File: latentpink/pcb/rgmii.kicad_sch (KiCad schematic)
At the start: 63 parts, among them J5 0826-1G1T-23-F, U2 XC7K160T-2FBG484C, U21 ECX2-LMV-3CN-125.000-TR, U22 ECS-2016MVQ-250-CN, U64 RCLAMP0514M, U65 RCLAMP0514M, U9 KSZ9031RN

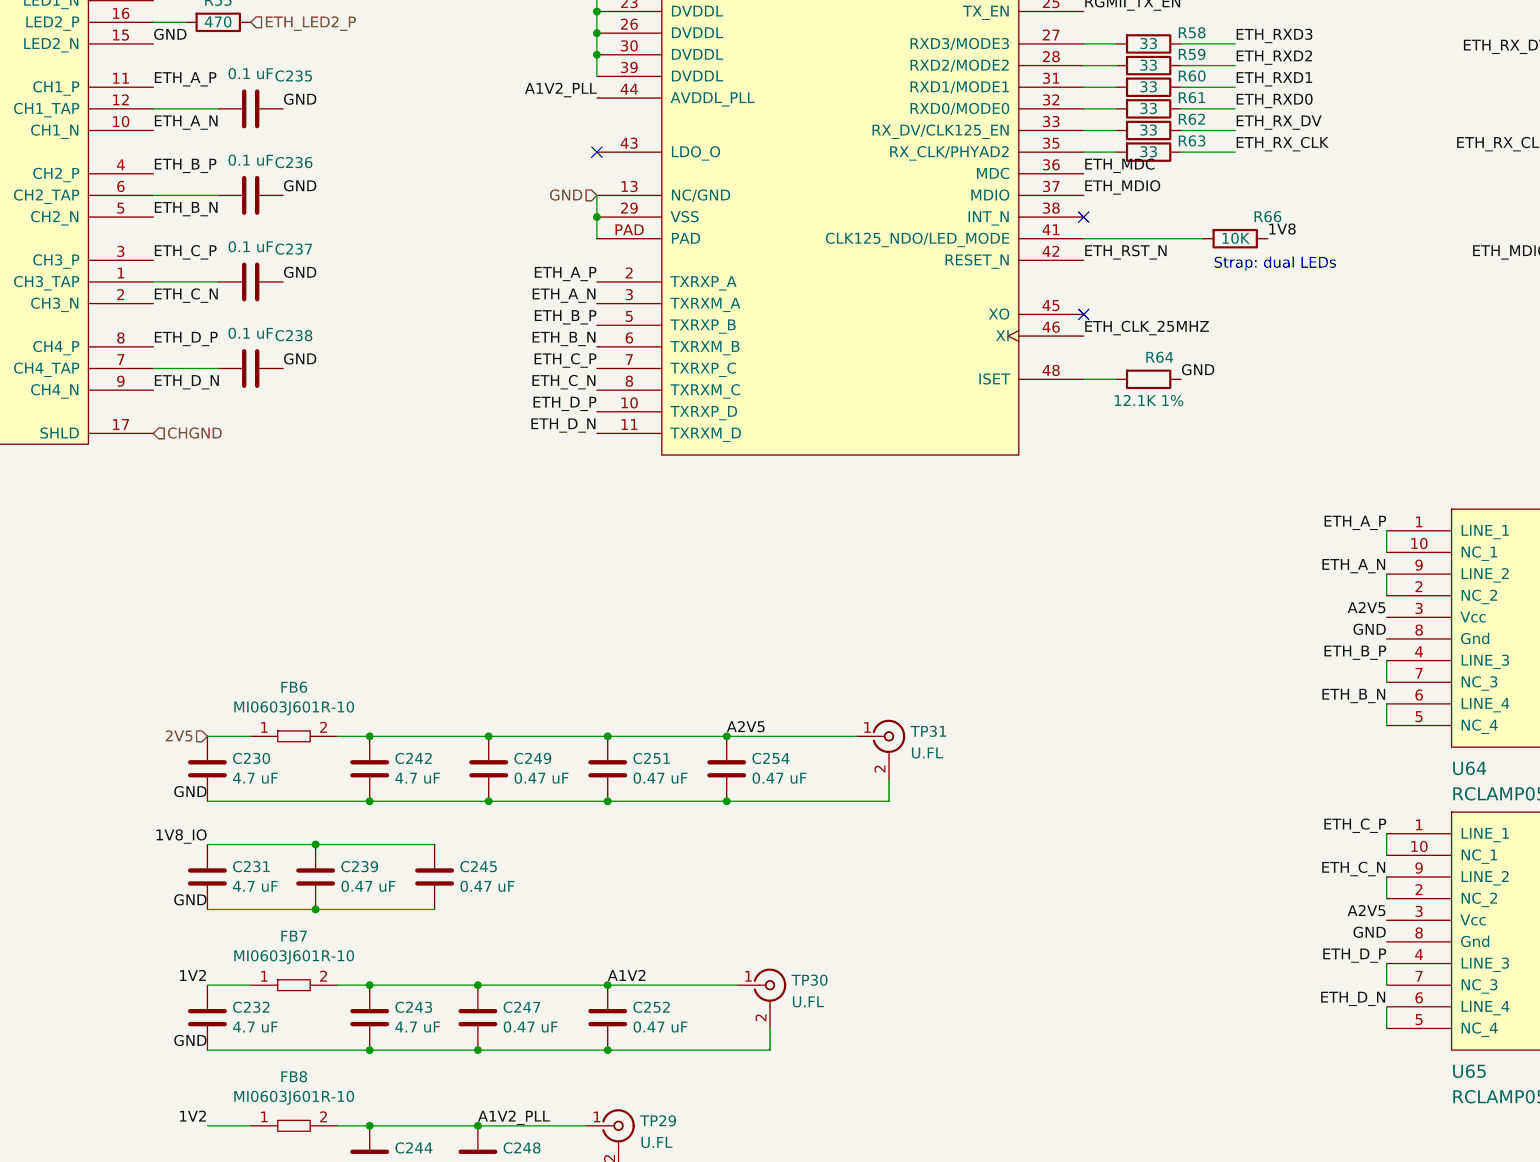
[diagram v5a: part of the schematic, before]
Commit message: Continued PHY layout
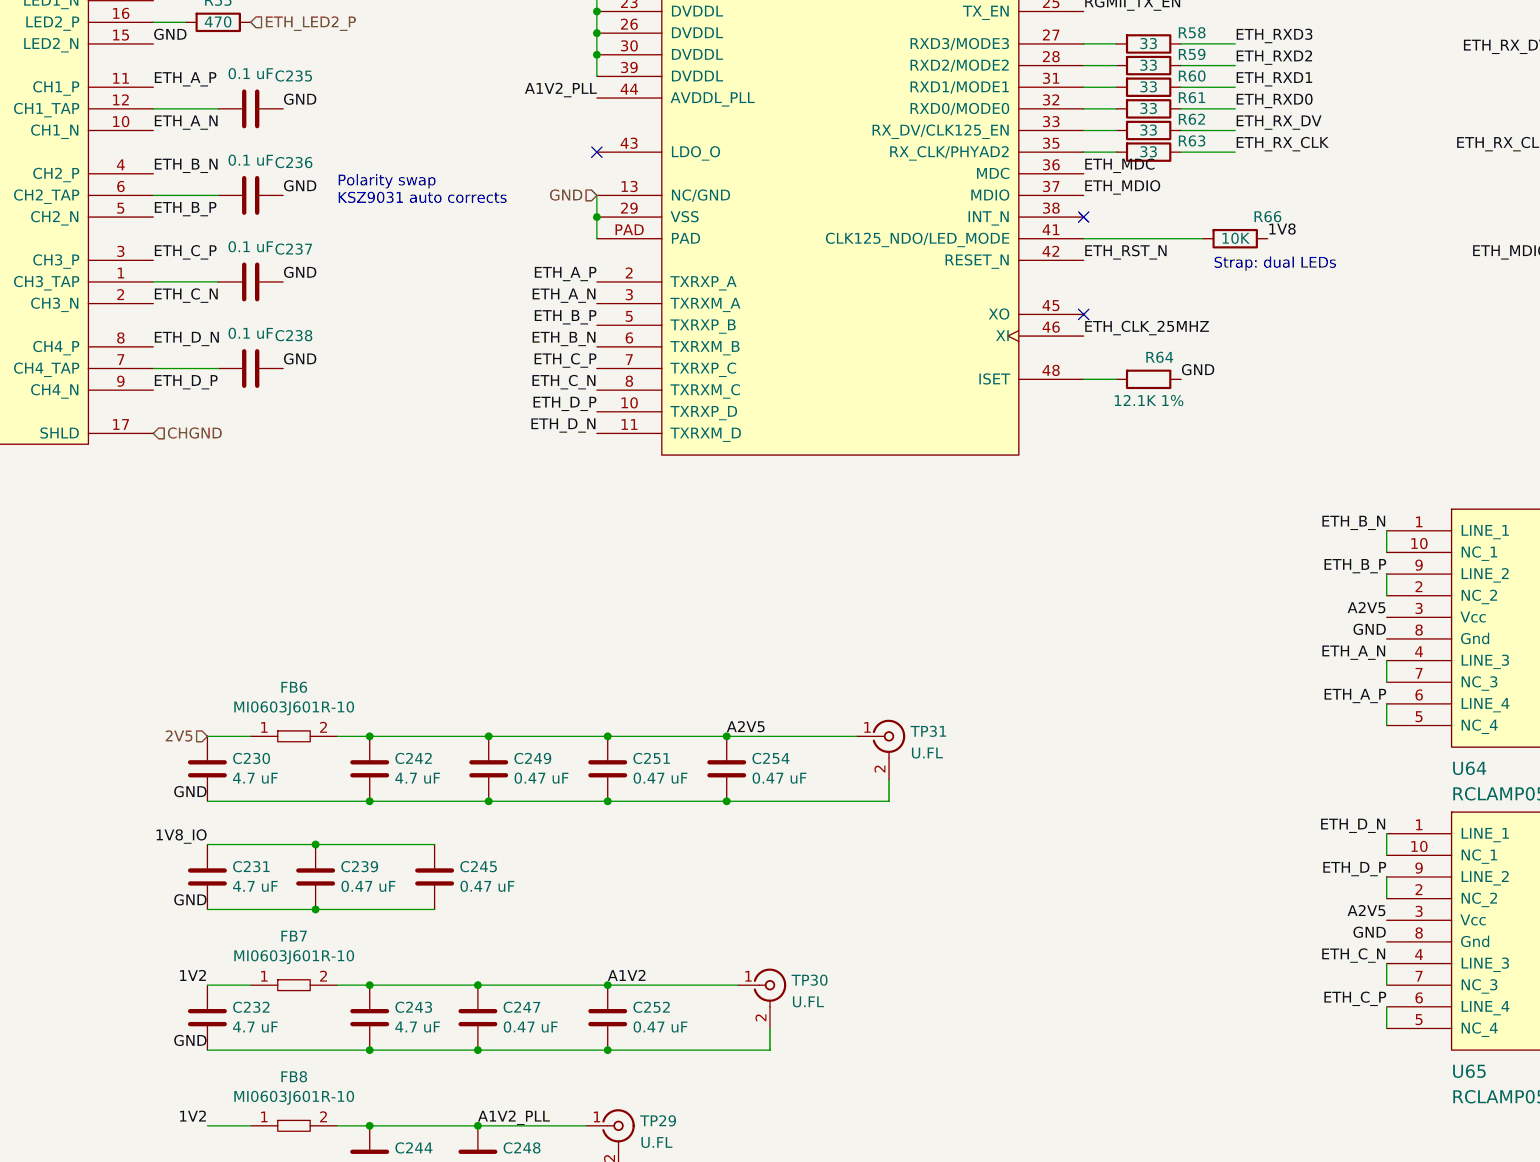
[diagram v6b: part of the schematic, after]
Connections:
- net ETH_A_N: now also U64.4 (LINE_3), U64.7 (NC_3); no longer U64.2 (NC_2), U64.9 (LINE_2)
- net ETH_A_P: now also U64.5 (NC_4), U64.6 (LINE_4); no longer U64.1 (LINE_1), U64.10 (NC_1)
- net ETH_B_N: now also J5.4 (CH2_P), U64.1 (LINE_1), U64.10 (NC_1); no longer J5.5 (CH2_N), U64.5 (NC_4), U64.6 (LINE_4)
- net ETH_B_P: now also J5.5 (CH2_N), U64.2 (NC_2), U64.9 (LINE_2); no longer J5.4 (CH2_P), U64.4 (LINE_3), U64.7 (NC_3)
- net ETH_C_N: now also U65.4 (LINE_3), U65.7 (NC_3); no longer U65.2 (NC_2), U65.9 (LINE_2)
- net ETH_C_P: now also U65.5 (NC_4), U65.6 (LINE_4); no longer U65.1 (LINE_1), U65.10 (NC_1)
- net ETH_D_N: now also J5.8 (CH4_P), U65.1 (LINE_1), U65.10 (NC_1); no longer J5.9 (CH4_N), U65.5 (NC_4), U65.6 (LINE_4)
- net ETH_D_P: now also J5.9 (CH4_N), U65.2 (NC_2), U65.9 (LINE_2); no longer J5.8 (CH4_P), U65.4 (LINE_3), U65.7 (NC_3)
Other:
- note added: "Polarity swap KSZ9031 auto corrects"
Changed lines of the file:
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@@
+    (effects (font (size 1.27 1.27)) (justify left bottom))
+  )
+  (text "Polarity swap\nKSZ9031 auto corrects" (at 64.77 73.66 0)
     (effects (font (size 1.27 1.27)) (justify left bottom))
   )
@@
     (effects (font (size 1.27 1.27)) (justify right bottom))
   )
-  (label "ETH_D_P" (at 187.96 162.56 180)
+  (label "ETH_D_P" (at 187.96 152.4 180)
     (effects (font (size 1.27 1.27)) (justify right bottom))
   )
@@
     (effects (font (size 1.27 1.27)) (justify right bottom))
   )
-  (label "ETH_B_P" (at 187.96 127 180)
-    (effects (font (size 1.27 1.27)) (justify right bottom))
-  )
-  (label "ETH_B_P" (at 43.18 69.85 0)
+  (label "ETH_B_P" (at 187.96 116.84 180)
+    (effects (font (size 1.27 1.27)) (justify right bottom))
+  )
+  (label "ETH_B_P" (at 43.18 74.93 0)
     (effects (font (size 1.27 1.27)) (justify left bottom))
   )
@@
     (effects (font (size 1.27 1.27)) (justify right bottom))
   )
-  (label "ETH_B_N" (at 187.96 132.08 180)
+  (label "ETH_B_N" (at 187.96 111.76 180)
     (effects (font (size 1.27 1.27)) (justify right bottom))
   )
@@
     (effects (font (size 1.27 1.27)) (justify left bottom))
   )
-  (label "ETH_D_N" (at 187.96 167.64 180)
+  (label "ETH_D_N" (at 187.96 147.32 180)
     (effects (font (size 1.27 1.27)) (justify right bottom))
   )
@@
     (effects (font (size 1.27 1.27)) (justify left bottom))
   )
-  (label "ETH_C_N" (at 187.96 152.4 180)
+  (label "ETH_C_N" (at 187.96 162.56 180)
     (effects (font (size 1.27 1.27)) (justify right bottom))
   )
@@
     (effects (font (size 1.27 1.27)) (justify right bottom))
   )
-  (label "ETH_A_N" (at 187.96 116.84 180)
+  (label "ETH_A_N" (at 187.96 127 180)
     (effects (font (size 1.27 1.27)) (justify right bottom))
   )
@@
     (effects (font (size 1.27 1.27)) (justify right bottom))
   )
-  (label "ETH_A_P" (at 187.96 111.76 180)
+  (label "ETH_A_P" (at 187.96 132.08 180)
     (effects (font (size 1.27 1.27)) (justify right bottom))
   )
@@
     (effects (font (size 1.27 1.27)) (justify right bottom))
   )
-  (label "ETH_C_P" (at 187.96 147.32 180)
+  (label "ETH_C_P" (at 187.96 167.64 180)
     (effects (font (size 1.27 1.27)) (justify right bottom))
   )
@@
     (effects (font (size 1.27 1.27)) (justify right bottom))
   )
-  (label "ETH_D_N" (at 43.18 95.25 0)
+  (label "ETH_D_N" (at 43.18 90.17 0)
     (effects (font (size 1.27 1.27)) (justify left bottom))
   )
@@
     (effects (font (size 1.27 1.27)) (justify right bottom))
   )
-  (label "ETH_D_P" (at 43.18 90.17 0)
+  (label "ETH_D_P" (at 43.18 95.25 0)
     (effects (font (size 1.27 1.27)) (justify left bottom))
   )
@@
     (effects (font (size 1.27 1.27)) (justify right bottom))
   )
-  (label "ETH_B_N" (at 43.18 74.93 0)
-    (effects (font (size 1.27 1.27)) (justify left bottom))
-  )
+  (label "ETH_B_N" (at 43.18 69.85 0)
+    (effects (font (size 1.27 1.27)) (justify left bottom))
+  )

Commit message: Lots more layout of low speed stuff and power. Partial layout of 1.2V supply. Initial RGMII escape routing.
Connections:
- net 1V8 is gone; now on net 1V8_IO: R66.1, R67.1, R68.1, R69.1, R73.1
- net ETH_LED1_N_1V8: no longer U2.L3 (IO_L1P_T0_34)
- net ETH_LED2_N_1V8: no longer U2.M3 (IO_L1N_T0_34)
- net ETH_MDC: now also U2.Y2 (IO_L21N_T3_DQS_34); no longer U2.P1 (IO_L8P_T1_34)
- net ETH_MDIO: now also U2.U1 (IO_L10N_T1_34); no longer U2.R1 (IO_L8N_T1_34)
- net ETH_RST_N: now also U2.W1 (IO_L20P_T3_34); no longer U2.M5 (IO_L9P_T1_DQS_34)
- net ETH_RXD0: now also U2.V2 (IO_L15N_T2_DQS_34); no longer U2.P4 (IO_L11P_T1_SRCC_34)
- net ETH_RXD1: now also U2.Y1 (IO_L20N_T3_34); no longer U2.U1 (IO_L10N_T1_34)
- net ETH_RXD2: now also U2.R2 (IO_L7N_T1_34); no longer U2.T1 (IO_L10P_T1_34)
- net ETH_RXD3: now also U2.Y3 (IO_L21P_T3_DQS_34); no longer U2.N4 (IO_L9N_T1_DQS_34)
- net ETH_RX_DV: now also U2.U2 (IO_L15P_T2_DQS_34); no longer U2.R4 (IO_L11N_T1_SRCC_34)
- net RGMII_TXD0: now also U2.AA1 (IO_L22P_T3_34); no longer U2.N3 (IO_L5P_T0_34)
- net RGMII_TXD1: now also U2.AB1 (IO_L22P_T3_34); no longer U2.N2 (IO_L5N_T0_34)
- net RGMII_TXD2: now also U2.AA3 (IO_L23P_T3_34); no longer U2.L5 (IO_L6P_T0_34)
- net RGMII_TXD3: now also U2.AB2 (IO_L23N_T3_34); no longer U2.L4 (IO_L6N_T0_VREF_34)
- net RGMII_TX_CLK: now also U2.W2 (IO_L17N_T2_34); no longer U2.P2 (IO_L7P_T1_34)
- net RGMII_TX_EN: now also U2.T1 (IO_L10P_T1_34); no longer U2.R2 (IO_L7N_T1_34)
- no-connect marks 30 -> 32
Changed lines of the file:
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@@
   (paper "A3")
   (title_block
-    (date "2023-05-31")
+    (date "2023-06-01")
   )
   (junction (at 95.25 53.34) (diameter 0) (color 0 0 0 0)
@@
   (junction (at 95.25 50.8) (diameter 0) (color 0 0 0 0)
   )
-  (no_connect (at 293.37 138.43))
   (no_connect (at 293.37 57.15))
   (no_connect (at 293.37 128.27))
   (no_connect (at 293.37 52.07))
-  (no_connect (at 293.37 146.05))
   (no_connect (at 293.37 54.61))
   (no_connect (at 152.4 74.93))
-  (no_connect (at 293.37 140.97))
+  (no_connect (at 293.37 69.85))
   (no_connect (at 293.37 133.35))
   (no_connect (at 293.37 120.65))
-  (no_connect (at 293.37 143.51))
-  (no_connect (at 293.37 113.03))
-  (no_connect (at 293.37 156.21))
+  (no_connect (at 293.37 80.01))
+  (no_connect (at 293.37 85.09))
+  (no_connect (at 293.37 135.89))
+  (no_connect (at 293.37 41.91))
   (no_connect (at 293.37 130.81))
-  (no_connect (at 293.37 151.13))
-  (no_connect (at 293.37 115.57))
+  (no_connect (at 293.37 67.31))
+  (no_connect (at 293.37 72.39))
   (no_connect (at 152.4 86.36))
   (no_connect (at 293.37 46.99))
-  (no_connect (at 293.37 135.89))
+  (no_connect (at 293.37 62.23))
+  (no_connect (at 293.37 92.71))
+  (no_connect (at 293.37 44.45))
   (no_connect (at 293.37 123.19))
-  (no_connect (at 293.37 153.67))
-  (no_connect (at 293.37 148.59))
+  (no_connect (at 293.37 64.77))
+  (no_connect (at 293.37 82.55))
+  (no_connect (at 293.37 77.47))
   (no_connect (at 293.37 107.95))
+  (no_connect (at 293.37 95.25))
   (no_connect (at 293.37 110.49))
-  (no_connect (at 293.37 125.73))
   (no_connect (at 293.37 118.11))
   (no_connect (at 95.25 67.31))
+  (no_connect (at 293.37 59.69))
   (no_connect (at 293.37 105.41))
-  (no_connect (at 293.37 59.69))
   (no_connect (at 293.37 49.53))
   (wire (pts (xy 90.17 201.93) (xy 104.14 201.93))
@@
     (effects (font (size 1.27 1.27)) (justify right bottom))
   )
-  (label "ETH_RXD3" (at 293.37 85.09 180)
-    (effects (font (size 1.27 1.27)) (justify right bottom))
-  )
-  (label "RGMII_TX_CLK" (at 293.37 72.39 180)
+  (label "ETH_RXD3" (at 293.37 143.51 180)
+    (effects (font (size 1.27 1.27)) (justify right bottom))
+  )
+  (label "RGMII_TX_CLK" (at 293.37 125.73 180)
     (effects (font (size 1.27 1.27)) (justify right bottom))
   )
@@
     (effects (font (size 1.27 1.27)) (justify right bottom))
   )
-  (label "ETH_RXD2" (at 293.37 87.63 180)
+  (label "ETH_RXD2" (at 293.37 74.93 180)
     (effects (font (size 1.27 1.27)) (justify right bottom))
   )
@@
     (effects (font (size 1.27 1.27)) (justify left bottom))
   )
-  (label "1V8" (at 219.71 36.83 0)
+  (label "1V8_IO" (at 219.71 36.83 0)
     (effects (font (size 1.27 1.27)) (justify left bottom))
   )
@@
     (effects (font (size 1.27 1.27)) (justify left bottom))
   )
-  (label "RGMII_TXD3" (at 293.37 69.85 180)
+  (label "RGMII_TXD3" (at 293.37 156.21 180)
     (effects (font (size 1.27 1.27)) (justify right bottom))
   )
@@
     (effects (font (size 1.27 1.27)) (justify right bottom))
   )
-  (label "1V8" (at 173.99 77.47 0)
-    (effects (font (size 1.27 1.27)) (justify left bottom))
-  )
-  (label "ETH_RXD1" (at 293.37 90.17 180)
+  (label "1V8_IO" (at 173.99 77.47 0)
+    (effects (font (size 1.27 1.27)) (justify left bottom))
+  )
+  (label "ETH_RXD1" (at 293.37 140.97 180)
     (effects (font (size 1.27 1.27)) (justify right bottom))
   )
@@
     (effects (font (size 1.27 1.27)) (justify right bottom))
   )
-  (label "RGMII_TX_EN" (at 293.37 74.93 180)
+  (label "RGMII_TX_EN" (at 293.37 87.63 180)
     (effects (font (size 1.27 1.27)) (justify right bottom))
   )
@@
     (effects (font (size 1.27 1.27)) (justify right bottom))
   )
-  (label "RGMII_TXD0" (at 293.37 62.23 180)
+  (label "RGMII_TXD0" (at 293.37 148.59 180)
     (effects (font (size 1.27 1.27)) (justify right bottom))
   )
@@
     (effects (font (size 1.27 1.27)) (justify right bottom))
   )
-  (label "1V8" (at 218.44 80.01 0)
+  (label "1V8_IO" (at 218.44 80.01 0)
     (effects (font (size 1.27 1.27)) (justify left bottom))
   )
@@
     (effects (font (size 1.27 1.27)) (justify left bottom))
   )
-  (label "ETH_LED2_N_1V8" (at 293.37 44.45 180)
-    (effects (font (size 1.27 1.27)) (justify right bottom))
-  )
   (label "ETH_A_P" (at 187.96 132.08 180)
     (effects (font (size 1.27 1.27)) (justify right bottom))
@@
     (effects (font (size 1.27 1.27)) (justify right bottom))
   )
-  (label "ETH_MDC" (at 293.37 77.47 180)
+  (label "ETH_MDC" (at 293.37 146.05 180)
     (effects (font (size 1.27 1.27)) (justify right bottom))
   )
@@
     (effects (font (size 1.27 1.27)) (justify right bottom))
   )
-  (label "RGMII_TXD1" (at 293.37 64.77 180)
+  (label "RGMII_TXD1" (at 293.37 151.13 180)
     (effects (font (size 1.27 1.27)) (justify right bottom))
   )
@@
     (effects (font (size 1.27 1.27)) (justify right bottom))
   )
-  (label "ETH_MDIO" (at 293.37 80.01 180)
+  (label "ETH_MDIO" (at 293.37 90.17 180)
     (effects (font (size 1.27 1.27)) (justify right bottom))
   )
@@
     (effects (font (size 1.27 1.27)) (justify right bottom))
   )
-  (label "ETH_RST_N" (at 293.37 82.55 180)
+  (label "ETH_RST_N" (at 293.37 138.43 180)
     (effects (font (size 1.27 1.27)) (justify right bottom))
   )
@@
     (effects (font (size 1.27 1.27)) (justify right bottom))
   )
-  (label "RGMII_TXD2" (at 293.37 67.31 180)
+  (label "RGMII_TXD2" (at 293.37 153.67 180)
     (effects (font (size 1.27 1.27)) (justify right bottom))
   )
@@
     (effects (font (size 1.27 1.27)) (justify left bottom))
   )
-  (label "ETH_RX_DV" (at 293.37 95.25 180)
+  (label "ETH_RX_DV" (at 293.37 113.03 180)
     (effects (font (size 1.27 1.27)) (justify right bottom))
   )
@@
     (effects (font (size 1.27 1.27)) (justify right bottom))
   )
-  (label "ETH_LED1_N_1V8" (at 293.37 41.91 180)
-    (effects (font (size 1.27 1.27)) (justify right bottom))
-  )
-  (label "ETH_RXD0" (at 293.37 92.71 180)
-    (effects (font (size 1.27 1.27)) (justify right bottom))
-  )
+  (label "ETH_RXD0" (at 293.37 115.57 180)
+    (effects (font (size 1.27 1.27)) (justify right bottom))
+  )
